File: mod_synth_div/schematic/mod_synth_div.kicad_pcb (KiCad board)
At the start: 2 copper layers, 50.8 x 109.2 mm, 68 parts, among them J1 In, J10 Conn_01x05_Female, J11 Conn_01x05_Male, J12 Conn_01x05_Female, J13 Conn_01x05_Male, J2 Rst, J3 Conn_02x08_Odd_Even, J4 1/2, J5 1/4, J6 1/8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

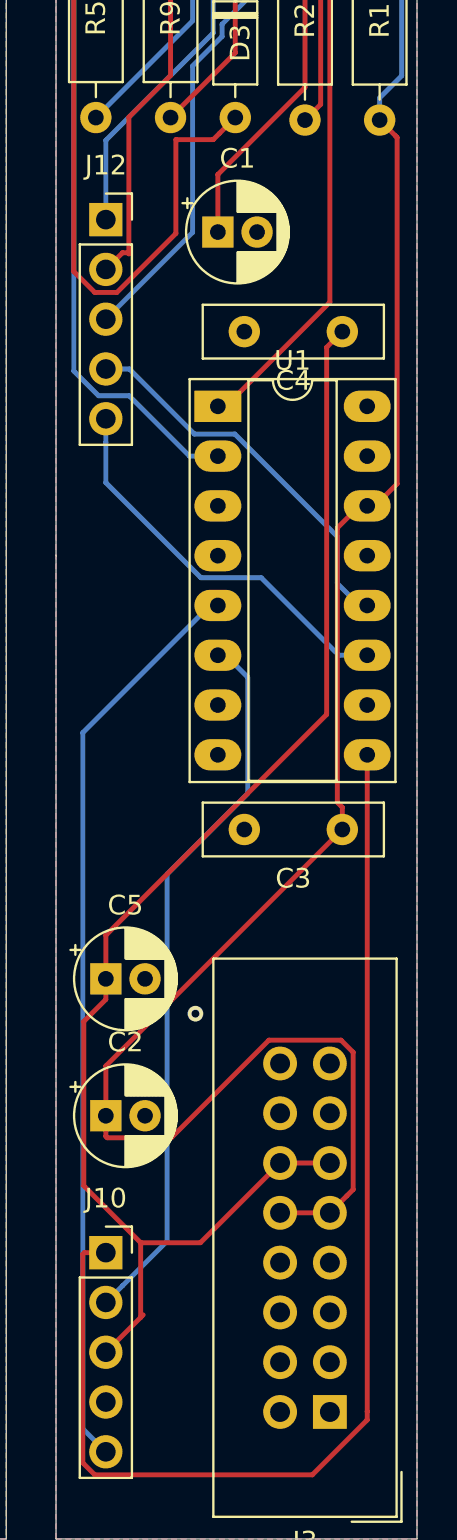
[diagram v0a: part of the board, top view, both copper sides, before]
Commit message: Use correct size socket
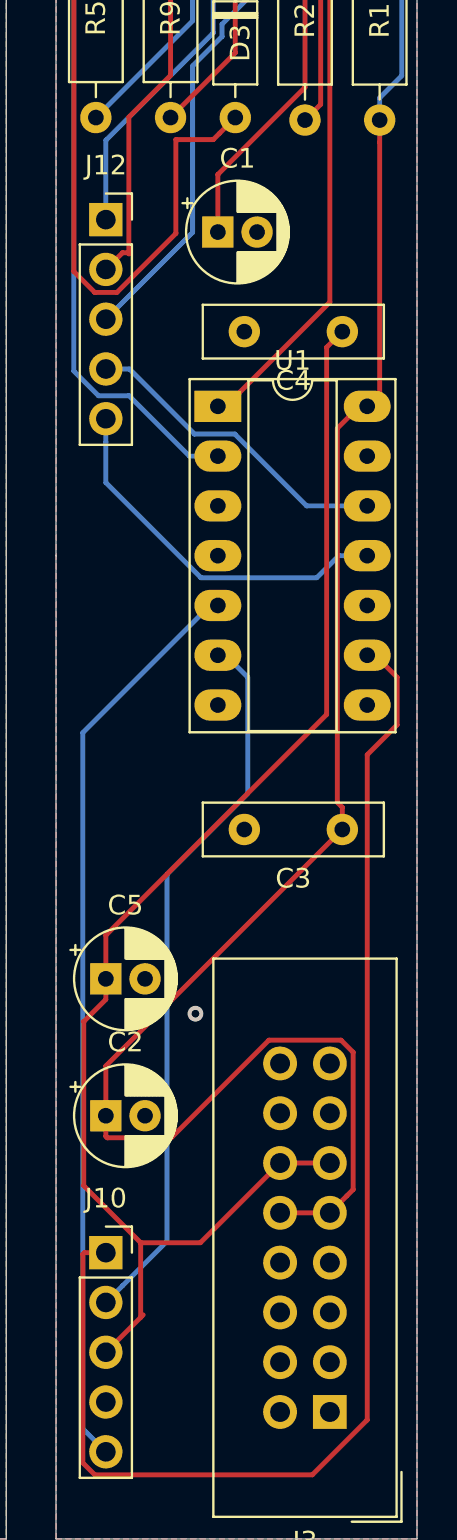
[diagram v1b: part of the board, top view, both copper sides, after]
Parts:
- U1: footprint Package_DIP:DIP-16_W7.62mm_Socket_LongPads -> Package_DIP:DIP-14_W7.62mm_Socket_LongPads
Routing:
- net /2_PCB_A: track 61.7 -> 68.3 mm
- net /0_PCB_A: track 19.7 -> 17.0 mm
- net /1_PCB_A: track 20.2 -> 19.1 mm
- net +12V: track 180.9 -> 180.2 mm
